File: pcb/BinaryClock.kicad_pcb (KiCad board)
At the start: 2 copper layers, 28.4 x 41.7 mm, 19 parts, among them CON1 AVR-ISP-6, CON2 BARREL_JACK, U1 MC33269, U2 DS3231, U3 clock_header, U4 clock_header, U6 ATMEGA328-AU, Y1 16MHz

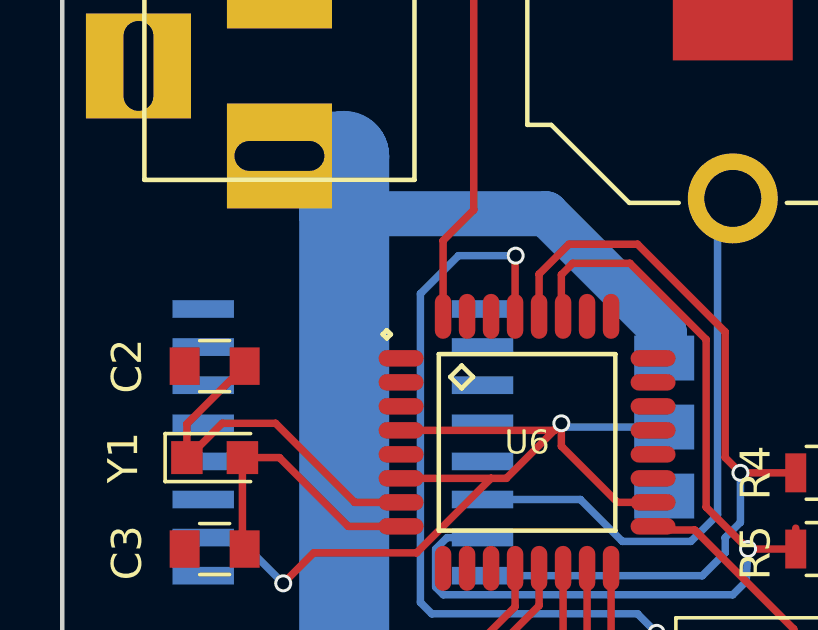
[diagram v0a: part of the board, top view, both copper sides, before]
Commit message: Added on-board pullup resistor for external on/off switch
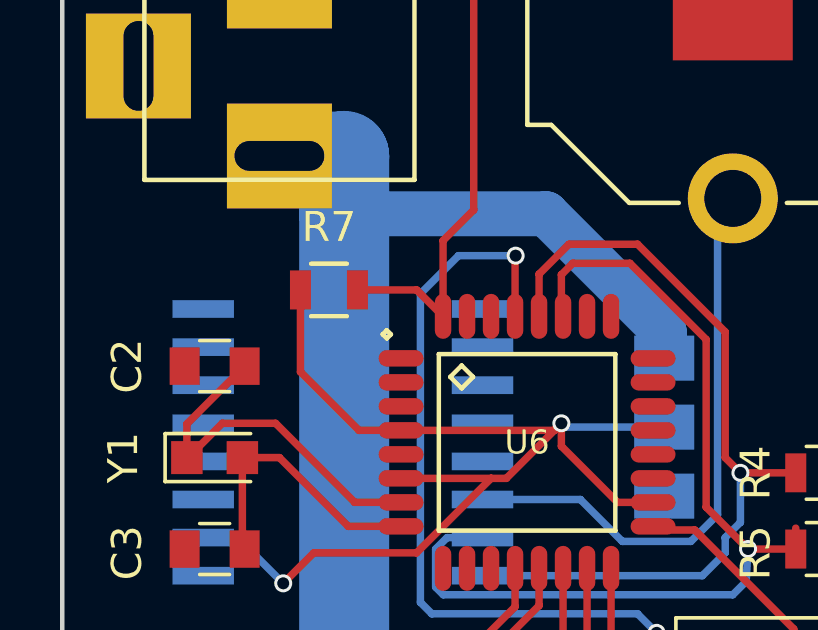
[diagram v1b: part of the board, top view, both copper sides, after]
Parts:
- added R7: 10k, Resistors_SMD:R_0805, F.Cu at (152.7, 75.2)
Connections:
- U6 pad 32: Net-(R7-Pad1) -> Net-(R7-Pad2)
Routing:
- net VCC: track 47.3 -> 54.2 mm
- net Net-(R7-Pad2): track 0.00 -> 5.74 mm
- net Net-(R7-Pad1): track 12.9 -> 10.3 mm
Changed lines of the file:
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@@
 (kicad_pcb (version 4) (host pcbnew 4.0.5)
   (general
-    (links 54)
+    (links 55)
     (no_connects 9)
     (area 143.688999 56.820999 172.287001 98.627001)
     (thickness 1.6)
     (drawings 14)
-    (tracks 160)
+    (tracks 165)
     (zones 0)
-    (modules 19)
-    (nets 38)
+    (modules 20)
+    (nets 39)
   )
   (page A4)
@@
   (net 36 "Net-(U6-Pad31)")
   (net 37 "Net-(U6-Pad9)")
+  (net 38 "Net-(R7-Pad2)")
   (net_class Default "This is the default net class."
     (clearance 0.2)
@@
     (add_net "Net-(R3-Pad2)")
     (add_net "Net-(R7-Pad1)")
+    (add_net "Net-(R7-Pad2)")
     (add_net "Net-(U2-Pad1)")
     (add_net "Net-(U2-Pad3)")
@@
       (net 36 "Net-(U6-Pad31)"))
     (pad 32 smd oval (at -2.8 -4.2) (size 0.55 1.5) (layers F.Cu F.Paste F.Mask)
-      (net 25 "Net-(R7-Pad1)"))
+      (net 38 "Net-(R7-Pad2)"))
     (model smd_lqfp/lqfp-32.wrl
       (at (xyz 0 0 0))
@@
     )
   )
+  (module Resistors_SMD:R_0805 (layer F.Cu)
+    (at 152.654 75.184)
+    (descr "Resistor SMD 0805, reflow soldering, Vishay (see dcrcw.pdf)")
+    (tags "resistor 0805")
+    (attr smd)
+    (fp_text reference R7 (at 0 -2.1) (layer F.SilkS)
+      (effects (font (size 1 1) (thickness 0.15)))
+    )
+    (fp_text value 10k (at 0 2.1) (layer F.Fab)
+      (effects (font (size 1 1) (thickness 0.15)))
+    )
+    (fp_line (start -1 0.625) (end -1 -0.625) (layer F.Fab) (width 0.1))
+    (fp_line (start 1 0.625) (end -1 0.625) (layer F.Fab) (width 0.1))
+    (fp_line (start 1 -0.625) (end 1 0.625) (layer F.Fab) (width 0.1))
+    (fp_line (start -1 -0.625) (end 1 -0.625) (layer F.Fab) (width 0.1))
+    (fp_line (start -1.6 -1) (end 1.6 -1) (layer F.CrtYd) (width 0.05))
+    (fp_line (start -1.6 1) (end 1.6 1) (layer F.CrtYd) (width 0.05))
+    (fp_line (start -1.6 -1) (end -1.6 1) (layer F.CrtYd) (width 0.05))
+    (fp_line (start 1.6 -1) (end 1.6 1) (layer F.CrtYd) (width 0.05))
+    (fp_line (start 0.6 0.875) (end -0.6 0.875) (layer F.SilkS) (width 0.15))
+    (fp_line (start -0.6 -0.875) (end 0.6 -0.875) (layer F.SilkS) (width 0.15))
+    (pad 1 smd rect (at -0.95 0) (size 0.7 1.3) (layers F.Cu F.Paste F.Mask)
+      (net 7 VCC))
+    (pad 2 smd rect (at 0.95 0) (size 0.7 1.3) (layers F.Cu F.Paste F.Mask)
+      (net 38 "Net-(R7-Pad2)"))
+    (model Resistors_SMD.3dshapes/R_0805.wrl
+      (at (xyz 0 0 0))
+      (scale (xyz 1 1 1))
+      (rotate (xyz 0 0 0))
+    )
+  )
   (gr_text @jinternetthings (at 153.543 91.186 180) (layer B.SilkS)
     (effects (font (size 1.5 1.5) (thickness 0.3)) (justify mirror))
@@
   (segment (start 165.735 95.123) (end 165.735 97.028) (width 0.25) (layer F.Cu) (net 6))
   (segment (start 163.002 92.39) (end 165.735 95.123) (width 0.25) (layer F.Cu) (net 6))
+  (segment (start 151.704 75.184) (end 151.704 77.917) (width 0.25) (layer F.Cu) (net 7) (status 400000))
+  (segment (start 153.651 79.864) (end 155.058 79.864) (width 0.25) (layer F.Cu) (net 7) (status 800000))
+  (segment (start 151.704 77.917) (end 153.651 79.864) (width 0.25) (layer F.Cu) (net 7))
   (segment (start 163.458 82.264) (end 162.274 82.264) (width 0.25) (layer F.Cu) (net 7))
   (segment (start 160.401 80.391) (end 160.401 79.629) (width 0.25) (layer F.Cu) (net 7))
@@
   (segment (start 160.458 90.42) (end 160.528 90.49) (width 0.25) (layer F.Cu) (net 22))
   (segment (start 157.48 63.627) (end 157.48 72.517) (width 0.25) (layer F.Cu) (net 25))
-  (segment (start 156.458 73.539) (end 156.458 76.064) (width 0.25) (layer F.Cu) (net 25))
   (segment (start 157.48 72.517) (end 156.458 73.539) (width 0.25) (layer F.Cu) (net 25))
+  (segment (start 153.604 75.184) (end 155.578 75.184) (width 0.25) (layer F.Cu) (net 38) (status 400000))
+  (segment (start 155.578 75.184) (end 156.458 76.064) (width 0.25) (layer F.Cu) (net 38) (status 800000))
+  (segment (start 156.458 73.539) (end 156.458 76.064) (width 0.25) (layer F.Cu) (net 38))
   (zone (net 1) (net_name GND) (layer B.Cu) (hatch edge 0.508)
     (connect_pads (clearance 0.508))

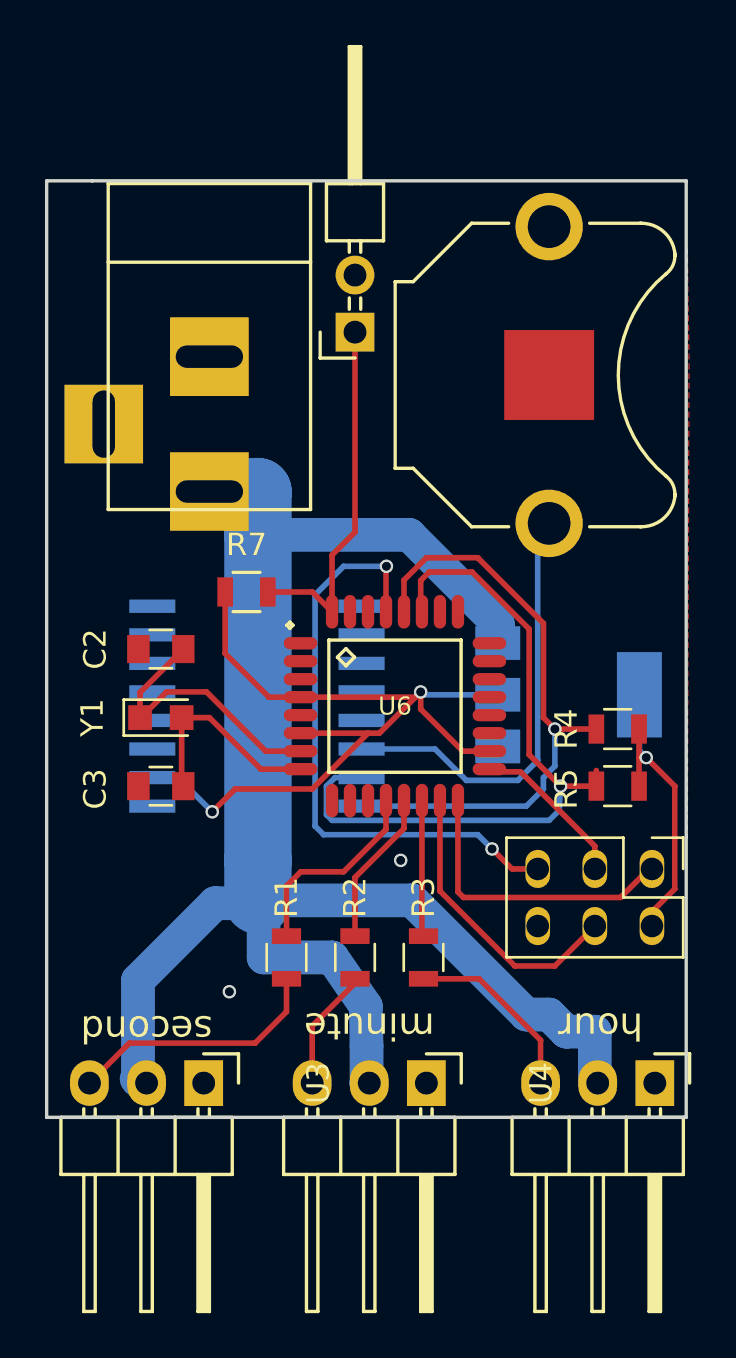
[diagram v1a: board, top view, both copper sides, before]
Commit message: Updated via sizes to increase annular rings
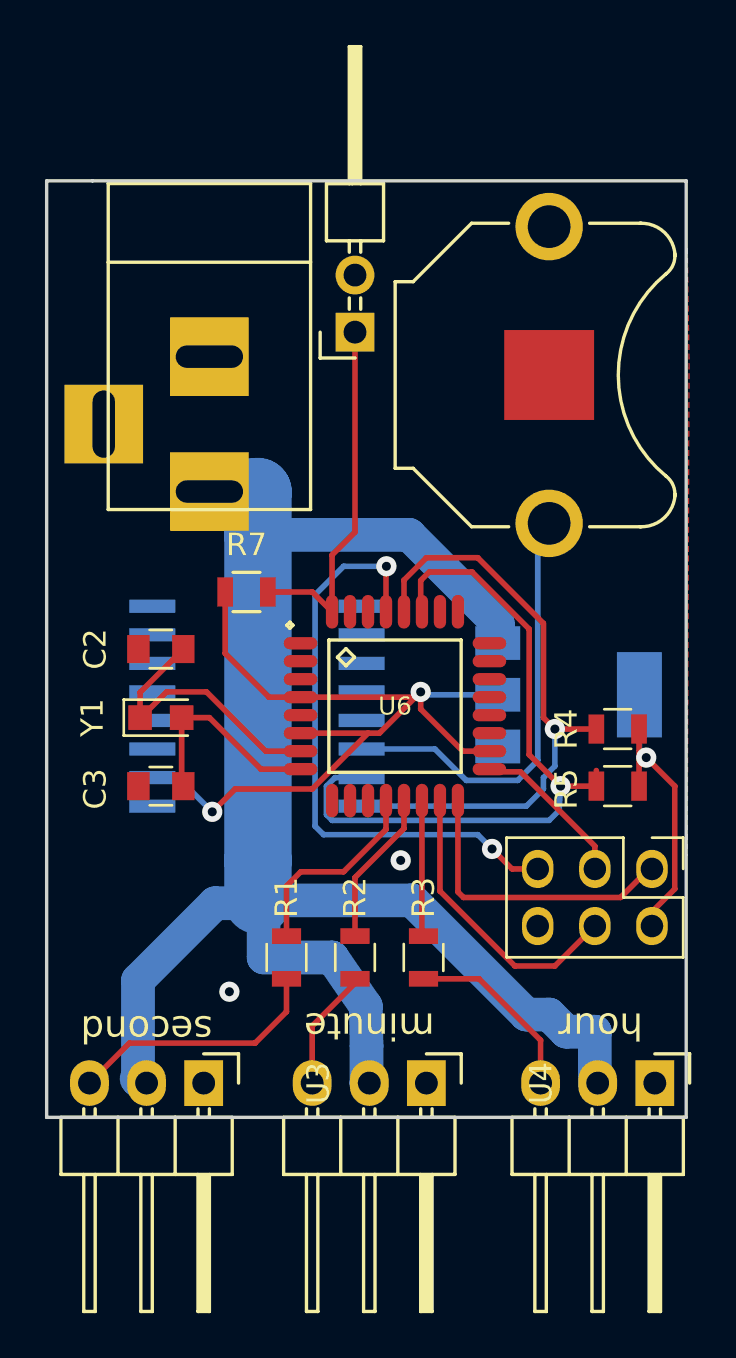
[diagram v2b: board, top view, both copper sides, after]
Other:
- rule via_min_size: 0.4 -> 0.6
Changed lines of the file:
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@@
     (via_size 0.6)
     (via_drill 0.4)
-    (via_min_size 0.4)
+    (via_min_size 0.6)
     (via_min_drill 0.3)
     (uvia_size 0.3)
@@
     (mod_text_size 1 1)
     (mod_text_width 0.15)
-    (pad_size 2.032 2.032)
-    (pad_drill 1.016)
+    (pad_size 1.7 1.4)
+    (pad_drill 1)
     (pad_to_mask_clearance 0.2)
     (aux_axis_origin 0 0)
@@
     (fp_line (start 4.1 6.6) (end 4.1 -1.6) (layer F.CrtYd) (width 0.05))
     (fp_line (start 4.1 -1.6) (end -1.6 -1.6) (layer F.CrtYd) (width 0.05))
-    (pad 1 thru_hole oval (at 0 0 270) (size 1.7 1.1) (drill 1) (layers *.Cu *.Mask)
+    (pad 1 thru_hole oval (at 0 0 270) (size 1.7 1.4) (drill 1) (layers *.Cu *.Mask)
       (net 11 /MISO))
-    (pad 2 thru_hole oval (at 2.54 0 270) (size 1.7 1.1) (drill 1) (layers *.Cu *.Mask)
+    (pad 2 thru_hole oval (at 2.54 0 270) (size 1.7 1.4) (drill 1) (layers *.Cu *.Mask)
       (net 7 VCC))
-    (pad 3 thru_hole oval (at 0 2.54 270) (size 1.7 1.1) (drill 1) (layers *.Cu *.Mask)
+    (pad 3 thru_hole oval (at 0 2.54 270) (size 1.7 1.4) (drill 1) (layers *.Cu *.Mask)
       (net 12 /SCK))
-    (pad 4 thru_hole oval (at 2.54 2.54 270) (size 1.7 1.1) (drill 1) (layers *.Cu *.Mask)
+    (pad 4 thru_hole oval (at 2.54 2.54 270) (size 1.7 1.4) (drill 1) (layers *.Cu *.Mask)
       (net 10 /MOSI))
-    (pad 5 thru_hole oval (at 0 5.08 270) (size 1.7 1.1) (drill 1) (layers *.Cu *.Mask)
+    (pad 5 thru_hole oval (at 0 5.08 270) (size 1.7 1.4) (drill 1) (layers *.Cu *.Mask)
       (net 13 /RESET))
-    (pad 6 thru_hole oval (at 2.54 5.08 270) (size 1.7 1.1) (drill 1) (layers *.Cu *.Mask)
+    (pad 6 thru_hole oval (at 2.54 5.08 270) (size 1.7 1.4) (drill 1) (layers *.Cu *.Mask)
       (net 1 GND))
     (model Pin_Headers.3dshapes/Pin_Header_Straight_2x03_Pitch2.54mm.wrl
@@
   (gr_line (start 172.212 56.896) (end 145.796 56.896) (angle 90) (layer Edge.Cuts) (width 0.15))
   (gr_line (start 172.212 98.552) (end 172.212 56.896) (angle 90) (layer Edge.Cuts) (width 0.15))
-  (via (at 159.512 87.122) (size 0.6) (drill 0.4) (layers F.Cu B.Cu) (net 0))
-  (via (at 151.892 92.964) (size 0.6) (drill 0.4) (layers F.Cu B.Cu) (net 0))
+  (via (at 159.512 87.122) (size 0.9) (drill 0.4) (layers F.Cu B.Cu) (net 0))
+  (via (at 151.892 92.964) (size 0.9) (drill 0.4) (layers F.Cu B.Cu) (net 0))
   (segment (start 147.919 80.772) (end 147.955 80.772) (width 0.25) (layer F.Cu) (net 2))
   (segment (start 147.955 80.772) (end 149.098 79.629) (width 0.25) (layer F.Cu) (net 2))
@@
   (segment (start 165.735 95.123) (end 165.735 97.028) (width 0.25) (layer F.Cu) (net 6))
   (segment (start 163.002 92.39) (end 165.735 95.123) (width 0.25) (layer F.Cu) (net 6))
-  (segment (start 151.704 75.184) (end 151.704 77.917) (width 0.25) (layer F.Cu) (net 7) (status 400000))
-  (segment (start 153.651 79.864) (end 155.058 79.864) (width 0.25) (layer F.Cu) (net 7) (status 800000))
+  (segment (start 151.704 75.184) (end 151.704 77.917) (width 0.25) (layer F.Cu) (net 7))
+  (segment (start 153.651 79.864) (end 155.058 79.864) (width 0.25) (layer F.Cu) (net 7))
   (segment (start 151.704 77.917) (end 153.651 79.864) (width 0.25) (layer F.Cu) (net 7))
   (segment (start 163.458 82.264) (end 162.274 82.264) (width 0.25) (layer F.Cu) (net 7))
@@
   (segment (start 152.146 83.947) (end 155.575 83.947) (width 0.25) (layer F.Cu) (net 7))
   (segment (start 151.13 84.963) (end 152.146 83.947) (width 0.25) (layer F.Cu) (net 7))
-  (via (at 151.13 84.963) (size 0.6) (drill 0.4) (layers F.Cu B.Cu) (net 7))
+  (via (at 151.13 84.963) (size 0.9) (drill 0.4) (layers F.Cu B.Cu) (net 7))
   (segment (start 149.606 83.439) (end 151.13 84.963) (width 0.25) (layer B.Cu) (net 7))
   (segment (start 170.688 90.043) (end 170.688 89.408) (width 0.25) (layer F.Cu) (net 7))
@@
   (segment (start 171.704 83.82) (end 170.434 82.55) (width 0.25) (layer F.Cu) (net 7))
   (segment (start 170.13 82.246) (end 170.13 79.756) (width 0.25) (layer B.Cu) (net 7))
-  (via (at 170.434 82.55) (size 0.6) (drill 0.4) (layers F.Cu B.Cu) (net 7))
+  (via (at 170.434 82.55) (size 0.9) (drill 0.4) (layers F.Cu B.Cu) (net 7))
   (segment (start 170.434 82.55) (end 170.13 82.246) (width 0.25) (layer B.Cu) (net 7))
   (segment (start 155.058 81.464) (end 158.058 81.464) (width 0.25) (layer F.Cu) (net 7))
@@
   (segment (start 160.166 79.864) (end 155.058 79.864) (width 0.25) (layer F.Cu) (net 7))
   (segment (start 160.401 79.629) (end 160.166 79.864) (width 0.25) (layer F.Cu) (net 7))
-  (via (at 160.401 79.629) (size 0.6) (drill 0.4) (layers F.Cu B.Cu) (net 7))
+  (via (at 160.401 79.629) (size 0.9) (drill 0.4) (layers F.Cu B.Cu) (net 7))
   (segment (start 160.528 79.756) (end 160.401 79.629) (width 0.25) (layer B.Cu) (net 7))
   (segment (start 149.479 83.439) (end 148.463 83.439) (width 0.25) (layer B.Cu) (net 7))
@@
   (segment (start 170.114 82.55) (end 170.114 83.82) (width 0.25) (layer F.Cu) (net 7))
   (segment (start 157.773 84.709) (end 165.1 84.709) (width 0.25) (layer B.Cu) (net 8))
-  (via (at 166.37 81.28) (size 0.6) (drill 0.4) (layers F.Cu B.Cu) (net 8))
+  (via (at 166.37 81.28) (size 0.9) (drill 0.4) (layers F.Cu B.Cu) (net 8))
   (segment (start 166.37 82.931) (end 166.37 81.28) (width 0.25) (layer B.Cu) (net 8))
   (segment (start 165.862 83.439) (end 166.37 82.931) (width 0.25) (layer B.Cu) (net 8))
@@
   (segment (start 166.37 81.28) (end 165.862 80.772) (width 0.25) (layer F.Cu) (net 8))
   (segment (start 166.116 85.344) (end 166.5605 84.8995) (width 0.25) (layer B.Cu) (net 9))
-  (via (at 166.624 83.82) (size 0.6) (drill 0.4) (layers F.Cu B.Cu) (net 9))
+  (via (at 166.624 83.82) (size 0.9) (drill 0.4) (layers F.Cu B.Cu) (net 9))
   (segment (start 166.5605 84.8995) (end 166.624 83.82) (width 0.25) (layer B.Cu) (net 9))
   (segment (start 168.214 83.82) (end 166.624 83.82) (width 0.25) (layer F.Cu) (net 9))
@@
   (segment (start 158.858 74.06) (end 158.858 76.064) (width 0.25) (layer F.Cu) (net 13))
   (segment (start 158.877 74.041) (end 158.858 74.06) (width 0.25) (layer F.Cu) (net 13))
-  (via (at 158.877 74.041) (size 0.6) (drill 0.4) (layers F.Cu B.Cu) (net 13))
+  (via (at 158.877 74.041) (size 0.9) (drill 0.4) (layers F.Cu B.Cu) (net 13))
   (segment (start 156.972 74.041) (end 158.877 74.041) (width 0.25) (layer B.Cu) (net 13))
   (segment (start 155.702 75.311) (end 156.972 74.041) (width 0.25) (layer B.Cu) (net 13))
@@
   (segment (start 162.941 85.979) (end 156.083 85.979) (width 0.25) (layer B.Cu) (net 13))
   (segment (start 163.576 86.614) (end 162.941 85.979) (width 0.25) (layer B.Cu) (net 13))
-  (via (at 163.576 86.614) (size 0.6) (drill 0.4) (layers F.Cu B.Cu) (net 13))
+  (via (at 163.576 86.614) (size 0.9) (drill 0.4) (layers F.Cu B.Cu) (net 13))
   (segment (start 164.465 87.503) (end 163.576 86.614) (width 0.25) (layer F.Cu) (net 13))
   (segment (start 153.162 70.739) (end 151.02586 70.739) (width 3) (layer B.Cu) (net 14))
@@
   (segment (start 157.48 63.627) (end 157.48 72.517) (width 0.25) (layer F.Cu) (net 25))
   (segment (start 157.48 72.517) (end 156.458 73.539) (width 0.25) (layer F.Cu) (net 25))
-  (segment (start 153.604 75.184) (end 155.578 75.184) (width 0.25) (layer F.Cu) (net 38) (status 400000))
-  (segment (start 155.578 75.184) (end 156.458 76.064) (width 0.25) (layer F.Cu) (net 38) (status 800000))
+  (segment (start 153.604 75.184) (end 155.578 75.184) (width 0.25) (layer F.Cu) (net 38))
+  (segment (start 155.578 75.184) (end 156.458 76.064) (width 0.25) (layer F.Cu) (net 38))
   (segment (start 156.458 73.539) (end 156.458 76.064) (width 0.25) (layer F.Cu) (net 38))
   (zone (net 1) (net_name GND) (layer B.Cu) (hatch edge 0.508)
